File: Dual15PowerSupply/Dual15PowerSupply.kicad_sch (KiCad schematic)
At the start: 17 parts, among them U1 LT3081, U2 LT3091xT7

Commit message: in work
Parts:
- added C5, C6: 100nF, Capacitor_THT:C_Rect_L7.2mm_W2.5mm_P5.00mm, symbol Device:C_US
- added C7, C8: 100µF, Capacitor_THT:CP_Radial_D8.0mm_P3.50mm, symbol Device:C_Polarized_US
- added D10, D9: LED, LED_THT:LED_D3.0mm, symbol Device:LED
- added R3: 5K, symbol Device:R_US
- added R4, R6: 300k, Resistor_SMD:R_1206_3216Metric_Pad1.30x1.75mm_HandSolder, symbol Device:R_US
- added R5: 1K, symbol Device:R_US
- added R7, R8: 1.8k, Resistor_THT:R_Axial_DIN0207_L6.3mm_D2.5mm_P15.24mm_Horizontal, symbol Device:R_US
- renumbered D3 to D2, D5 to D3, D7 to D4, D2 to D5, D4 to D6, D6 to D7
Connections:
- net GND: now also U2.2 (IMONN), U2.6 (GND), C5.2, C6.1, C7.2, C8.1, R3.2, R4.2, R5.2, R6.1
- net at U2.1 (ILIM): now also C4.2, R2.1, U2.3 (~{SHDN}), U2.4 (IN)
- net at U2.5 (SET): now also C6.2, R6.2
- net at U2.7 (OUT): now also C8.2, D10.1 (K)
- net at U1.2 (SET): now also C5.1, R4.1
- net at U1.3 (Imon): now also R3.1
- net at U1.4 (OUT): now also C7.1, D9.2 (A)
- net at U1.5 (TEMP): now also R5.1
- new net: D10.2 (A), R8.2
- new net: R7.2, R8.1
- new net: D9.1 (K), R7.1
- no-connect marks 0 -> 1
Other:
- note added: "1.8kΩ ~ 7mA"
- note added: "Guard rings tied to Vout around SET pins"
- moved on the sheet: R1, U1, U2

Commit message: More
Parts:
- added J1: 117VAC In, symbol Connector:Screw_Terminal_01x02
- added R9: 2k, symbol Device:R_US
- added TP1: 1mV/C, symbol Connector:TestPoint
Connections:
- net GND: now also R7.2, R8.1, R9.1; no longer U2.2 (IMONN)
- net at TR1.1: now also TR1.3, J1.2 (Pin_2)
- net at TR1.2: now also TR1.4, J1.1 (Pin_1)
- net at TR1.6: now also D7.2 (A), D8.1 (K)
- net at R5.1, U1.5 (TEMP): now also TP1.1
- new net: R9.2, U2.2 (IMONN)
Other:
- note added: "1mV/mA"
- moved on the sheet: R5

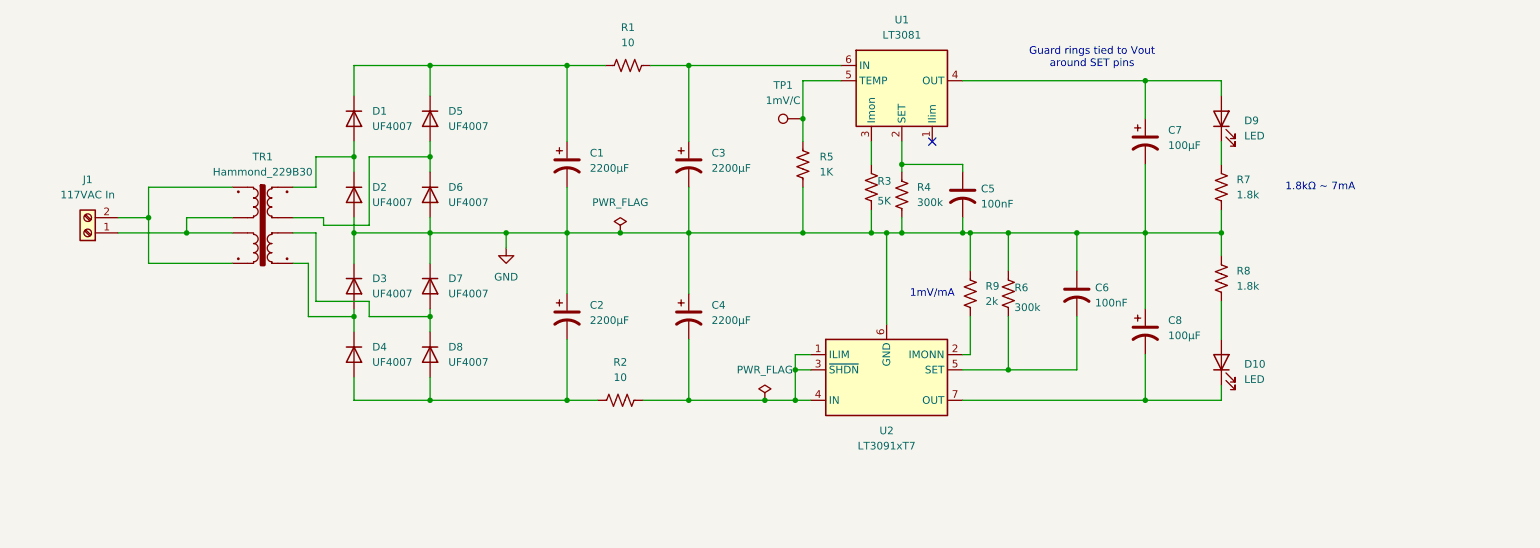
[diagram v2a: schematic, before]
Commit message: added current limit resistors.
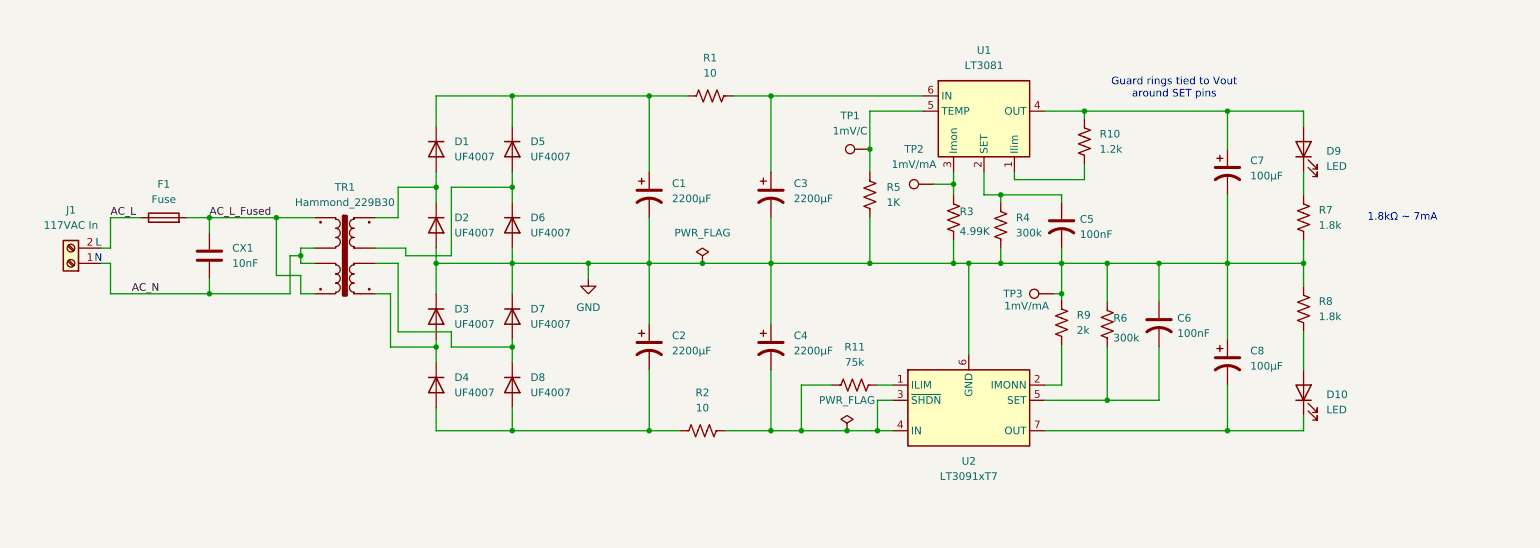
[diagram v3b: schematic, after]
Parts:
- added CX1: 10nF, Capacitor_THT:C_Rect_L13.0mm_W4.0mm_P10.00mm_FKS3_FKP3_MKS4, symbol Device:C
- added F1: Fuse, symbol Device:Fuse
- added R10: 1.2k, symbol Device:R_US
- added R11: 75k, symbol Device:R_US
- added TP2, TP3: 1mV/mA, symbol Connector:TestPoint
- C2: footprint (none) -> Capacitor_THT:CP_Radial_D16.0mm_P7.50mm; MPN (none) -> UPW1V222MHD; Mouser (none) -> 647-UPW1V222MHD
- R1, R2: footprint (none) -> Resistor_THT:R_Axial_DIN0414_L11.9mm_D4.5mm_P20.32mm_Horizontal; MPN (none) -> MOS2CT52R10R0F; Mouser (none) -> 660-MOS2CT52R10R0F
- R3: value 5K -> 4.99K; footprint (none) -> Resistor_SMD:R_1206_3216Metric_Pad1.30x1.75mm_HandSolder; MPN (none) -> RC1206FR-074K99L; Mouser (none) -> 603-RC1206FR-074K99L
- R5: footprint (none) -> Resistor_SMD:R_1206_3216Metric_Pad1.30x1.75mm_HandSolder; MPN (none) -> RC1206FR-101KL; Mouser (none) -> 603-RC1206FR-101KL
- U1: footprint (none) -> Package_TO_SOT_THT:TO-220-7_P2.54x5.08mm_StaggerOdd_Lead3.08mm_Vertical; MPN (none) -> LT3081ET7; Mouser (none) -> 584-LT3081ET7#PBF
- U2: Mouser (none) -> 584-LT3091ET7#PBF
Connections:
- net GND: now also TP3.1
- net AC_N: now reaches J1.1 (Pin_1), TR1.2, TR1.4
- net AC_N: now also CX1.2
- net AC_L_Fused: now reaches TR1.1, TR1.3
- net AC_L_Fused: now also CX1.1, F1.2; no longer J1.2 (Pin_2)
- net at C4.2, R2.1, U2.3 (~{SHDN})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: now also R11.1; no longer U2.1 (ILIM)
- net at U1.1 (Ilim): now also R10.2
- net at R3.1, U1.3 (Imon): now also TP2.1
- net at C7.1, D9.2 (A), U1.4 (OUT): now also R10.1
- new net: R11.2, U2.1 (ILIM)
- new net AC_L: F1.1, J1.2 (Pin_2)
- no-connect marks 1 -> 0
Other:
- note added: "L"
- note added: "N"
- note removed: "1mV/mA"
- moved on the sheet: C1, C3, C4, C5, C6, C7, C8, D1, D10, D2, D3, D4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

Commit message: Move datasheets.  A bit more capture work
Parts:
- F1: MPN (none) -> 696105003002; Mouser (none) -> 710-696105003002
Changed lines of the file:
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@@
 			)
 		)
-		(property "Datasheet" ""
+		(property "Datasheet" "https://www.we-online.com/components/products/datasheet/696105003002.pdf"
 			(at 39.37 50.8 0)
 			(hide yes)
@@
 			)
 		)
-		(property "Description" "Fuse"
+		(property "Description" "Fuseholder, Würth WR-FSH, 5 mm x 20 mm"
 			(at 39.37 50.8 0)
 			(hide yes)
 			(show_name no)
+			(do_not_autoplace no)
+			(effects
+				(font
+					(size 1.27 1.27)
+				)
+			)
+		)
+		(property "MPN" "696105003002"
+			(at 39.37 50.8 90)
+			(hide yes)
+			(show_name no)
+			(do_not_autoplace no)
+			(effects
+				(font
+					(size 1.27 1.27)
+				)
+			)
+		)
+		(property "Mouser" "710-696105003002 "
+			(at 39.37 50.8 90)
+			(hide yes)
+			(show_name no)

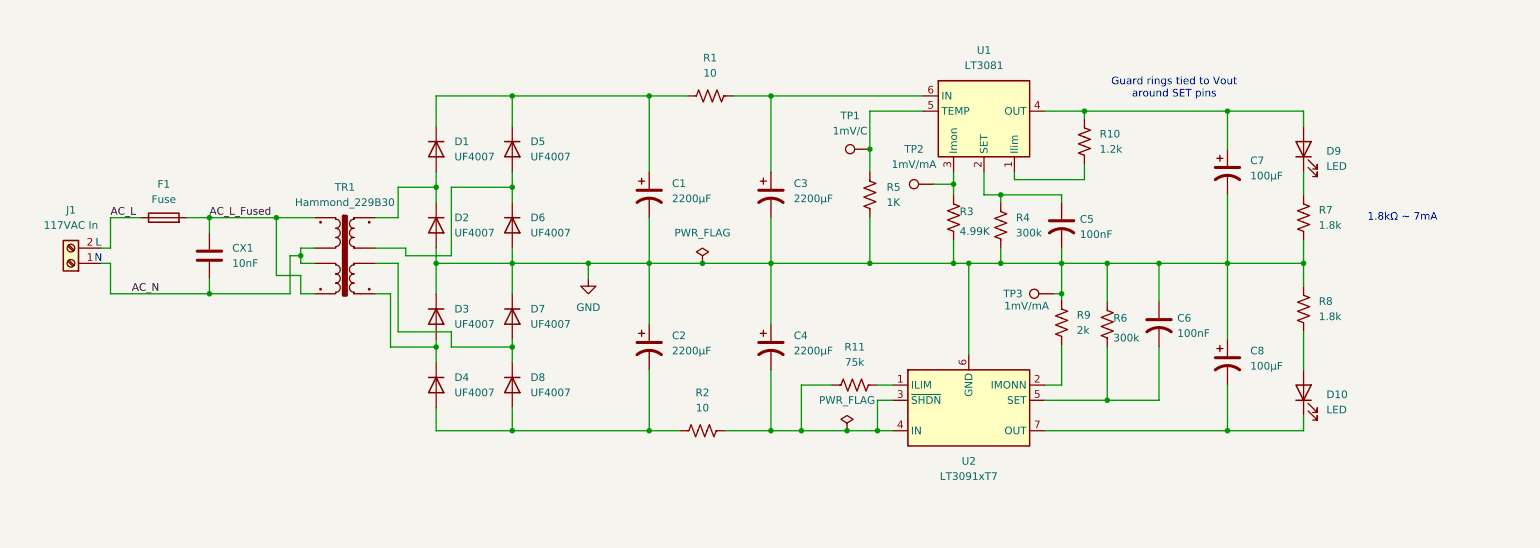
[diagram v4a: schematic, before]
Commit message: Adding footprints to project.
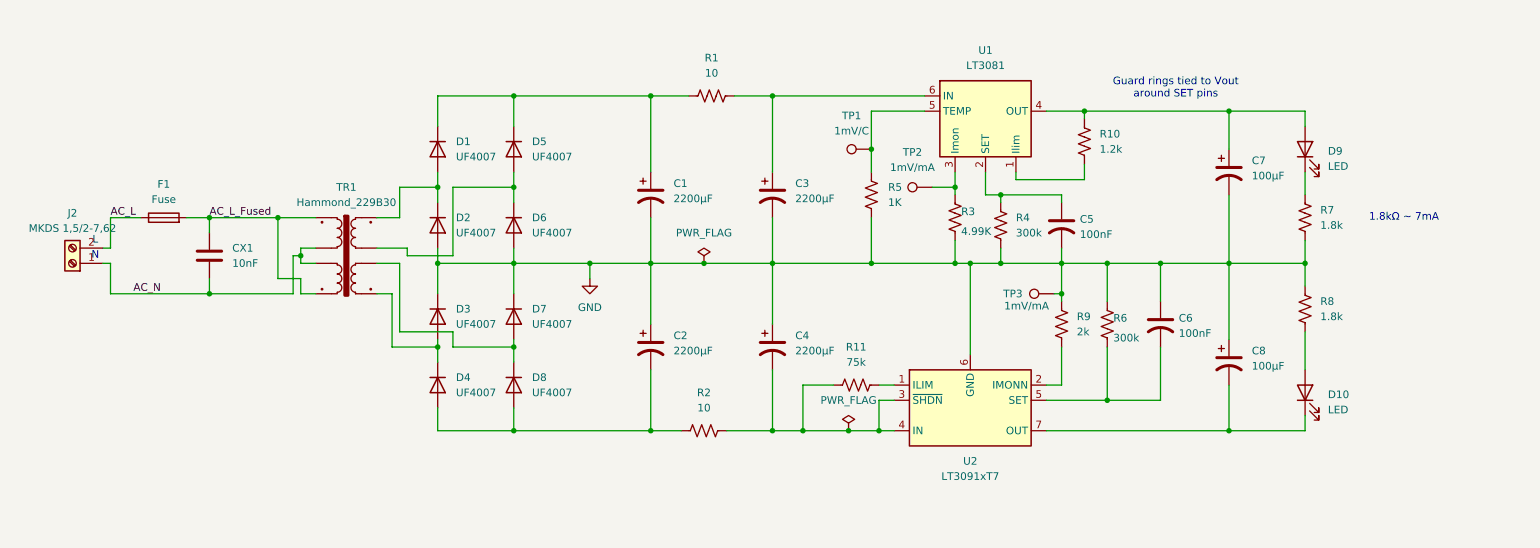
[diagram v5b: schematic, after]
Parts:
- removed J1: 117VAC In, symbol Connector:Screw_Terminal_01x02
- added J2: MKDS 1,5/2-7,62, TerminalBlock_762:MKDS 5_2-7,62, symbol Connector:Screw_Terminal_01x02
- F1: footprint (none) -> Fuseholder_Wurth:Wurth_WR-FSH_696105003002
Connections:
- net AC_L: now also J2.2 (Pin_2)
- net AC_N: now also J2.1 (Pin_1)
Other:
- moved on the sheet: TP2

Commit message: Getting ready for first pass at layout
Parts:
- J1: renamed from J2; MPN (none) -> 1717729; Mouser (none) -> 651-1717729
- R3: renamed from R11; footprint (none) -> Resistor_SMD:R_1206_3216Metric_Pad1.30x1.75mm_HandSolder; MPN (none) -> RE1206FRE0775KL; Mouser (none) -> 603-RE1206FRE0775KL
- R7: renamed from R9; footprint (none) -> Resistor_SMD:R_1206_3216Metric_Pad1.30x1.75mm_HandSolder; MPN (none) -> RT1206FRE072KL; Mouser (none) -> 603-RT1206FRE072KL
- R8: renamed from R10; footprint (none) -> Resistor_SMD:R_1206_3216Metric_Pad1.30x1.75mm_HandSolder; MPN (none) -> RT1206FRE071K2L; Mouser (none) -> 603-RT1206FRE071K2L
- TP1, TP2, TP3: footprint (none) -> TestPoint:TestPoint_Keystone_5005-5009_Compact
- TR1: footprint (none) -> Transformer_Hammond_229:Hammond_229B30_RoundDrill; MPN (none) -> 229B30; Mouser (none) -> 546-229B30-BULK
- renumbered R2 to R1, R7 to R10, R8 to R11, R1 to R2, R5 to R4, R3 to R5, R4 to R6, R6 to R9, U2 to U1, U1 to U2
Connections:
- net GND: no longer TP3.1
- net at R7.2, U1.2 (IMONN): now also TP3.1
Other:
- moved on the sheet: R7, TP3

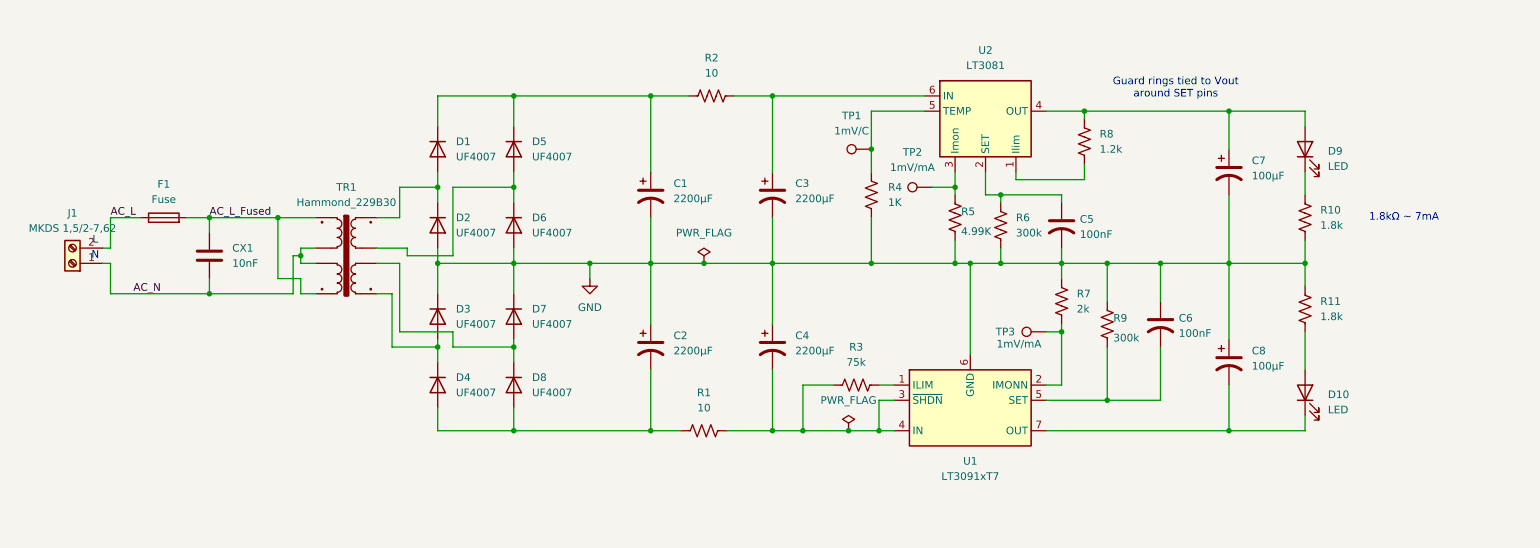
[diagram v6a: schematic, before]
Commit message: Post schematic design review first pass.
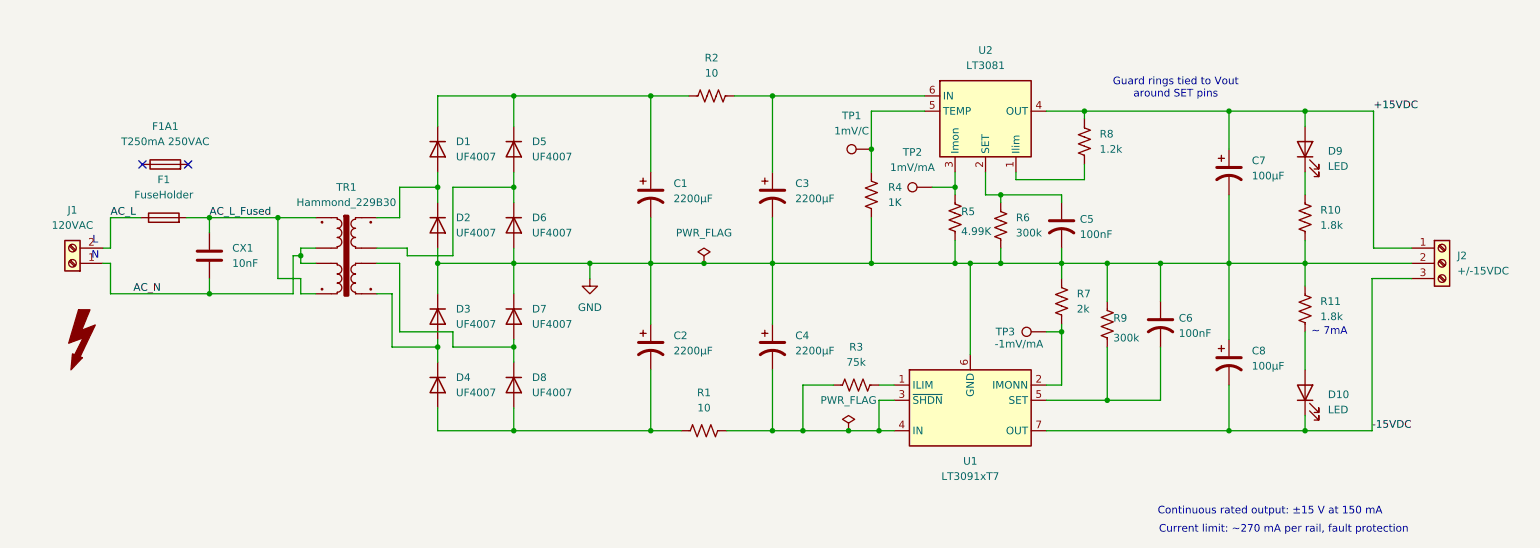
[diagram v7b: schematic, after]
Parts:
- added F1A1: T250mA 250VAC, symbol Device:Fuse
- added J2: +/-15VDC, TerminalBlock_Phoenix:TerminalBlock_Phoenix_MKDS-3-3-5.08_1x03_P5.08mm_Horizontal, symbol Connector:Screw_Terminal_01x03
- F1: value Fuse -> FuseHolder
- J1: value MKDS 1,5/2-7,62 -> 120VAC
- TP3: value 1mV/mA -> -1mV/mA
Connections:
- net GND: now also J2.2 (Pin_2)
- net -15VDC: now reaches C8.2, D10.1 (K), U1.7 (OUT)
- net -15VDC: now also J2.3 (Pin_3)
- net +15VDC: now reaches C7.1, D9.2 (A), R8.1, U2.4 (OUT)
- net +15VDC: now also J2.1 (Pin_1)
- no-connect marks 0 -> 2
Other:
- note added: "Continuous rated output: ±15 V at 150 mA"
- note added: "Current limit: ~270 mA per rail, fault protection"
- note added: "~ 7mA"
- note removed: "1.8kΩ ~ 7mA"
